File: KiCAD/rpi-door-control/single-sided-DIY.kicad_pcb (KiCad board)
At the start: 2 copper layers, 123 x 50 mm, 26 parts, among them IC1 4N35, J1 RJ45, P1 CONN_13X2, P2 CONN_2, P3 CONN_2, P4 CONN_2, Q1 2N3904, Q2 2N3904, SW1 SW_PUSH, U1 RELAY

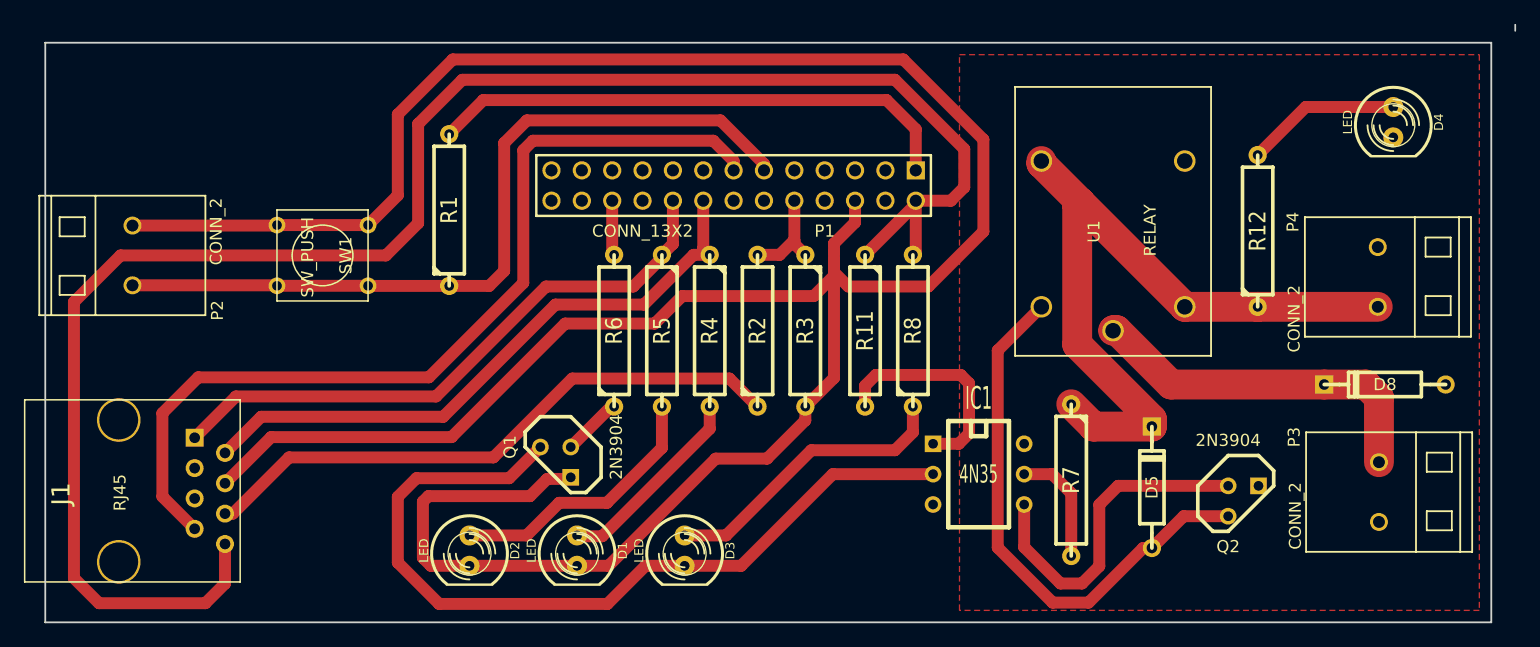
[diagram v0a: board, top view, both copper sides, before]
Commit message: Added silk screen text, drill holes, general polishing
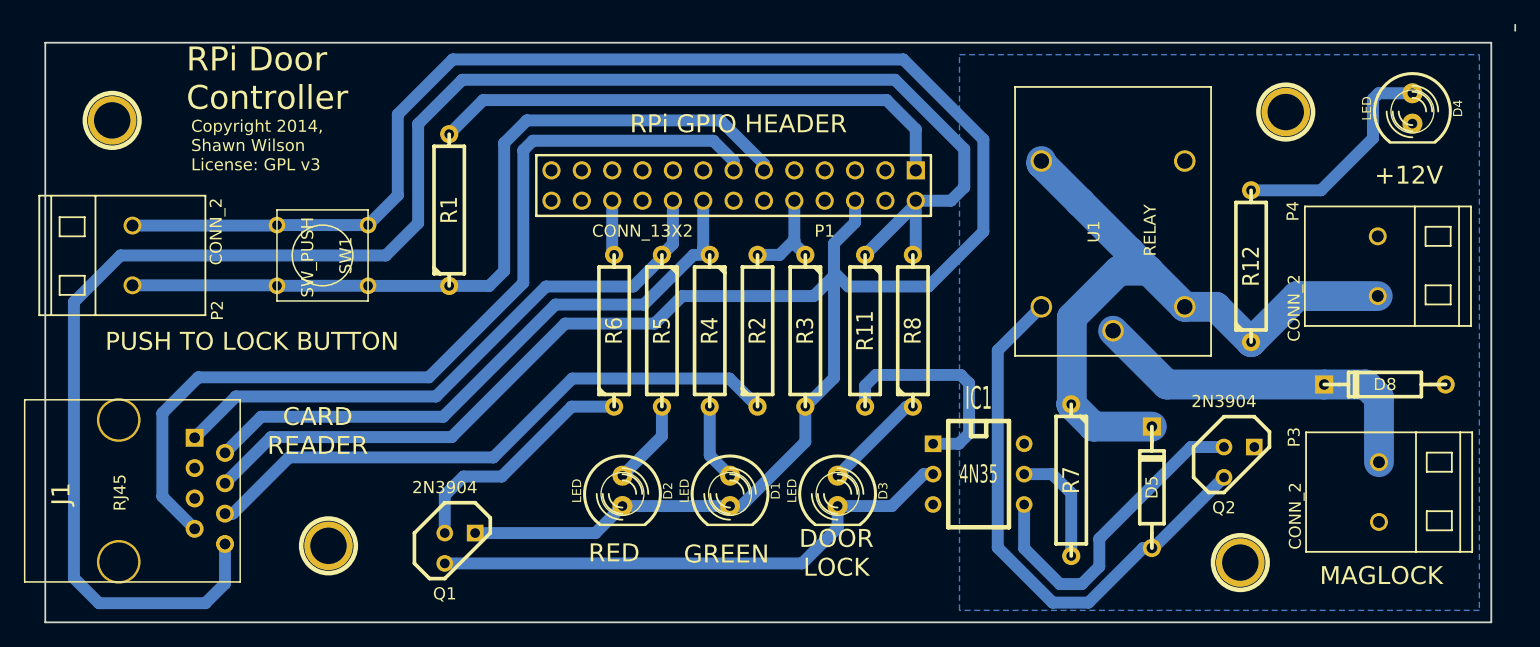
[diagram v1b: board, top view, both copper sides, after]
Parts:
- added ?: , 1pin, F.Cu at (180.0, 121.0)
- added ?: , 1pin, F.Cu at (103.7, 119.6)
- added ?: , 1pin, F.Cu at (183.8, 83.3)
- added ?: , 1pin, F.Cu at (85.6, 84.0)
- moved D1 13.7 mm to (137.3, 115.0)
- moved D2 13.7 mm to (128.3, 115.0)
- moved D3 13.7 mm to (146.3, 115.0)
- moved Q1 10.8 mm to (114.7, 119.8), turned to 0 degrees
- moved Q2 3.27 mm to (179.9, 112.6)
- moved R12 3.00 mm to (180.9, 96.2)
- moved D4 1.97 mm to (194.4, 83.0)
- moved P4 0.90 mm to (191.5, 96.2)
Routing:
- net N-0000025: track 69.9 -> 45.0 mm
- net GND: track 241.9 -> 219.2 mm
- net N-0000026: track 24.8 -> 8.69 mm
- net N-000001: track 22.6 -> 7.15 mm
- net N-000003: track 5.03 -> 20.4 mm
- net N-000002: track 16.7 -> 6.48 mm
- net N-0000021: track 13.0 -> 18.8 mm
- net +12V: track 62.3 -> 59.1 mm
- net N-0000038: track 45.8 -> 46.8 mm
- net N-0000020: track 28.3 -> 27.7 mm
- added copper zone on B.Cu, net GNDPWR
- removed copper zone on F.Cu, net GNDPWR
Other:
- board text added: "+12V"
- board text added: "CARD READER"
- board text added: "Copyright 2014, Shawn Wilson License: GPL v3"
- board text added: "DOOR LOCK"
- board text added: "GREEN"
- board text added: "MAGLOCK"
- board text added: "PUSH TO LOCK BUTTON"
- board text added: "RED"
- board text added: "RPi Door Controller"
- board text added: "RPi GPIO HEADER"

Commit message: Got 3D model for terminal blocks working.  Still need to change the colour of the skin but they do show up in the KiCAD 3D view.
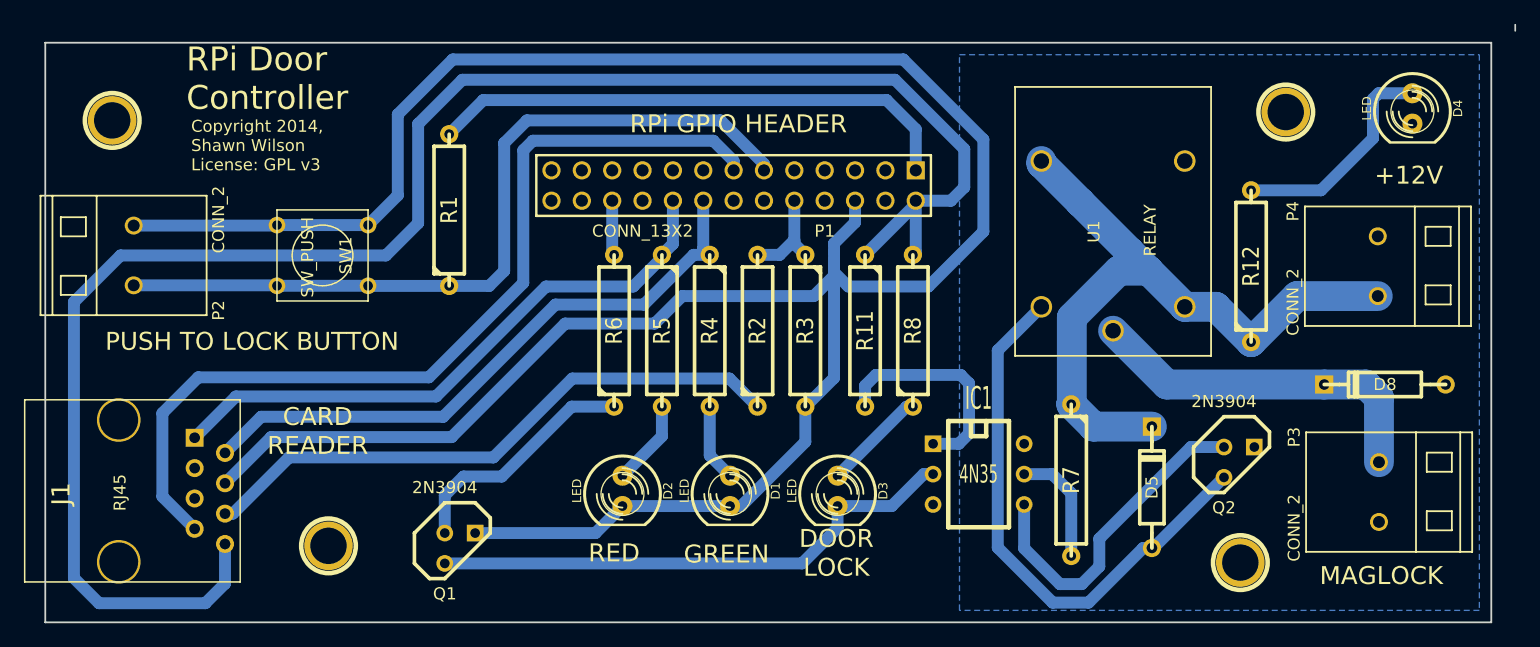
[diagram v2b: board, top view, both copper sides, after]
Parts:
- moved P2 0.10 mm to (87.4, 95.3)
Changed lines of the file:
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@@
     (links 48)
     (no_connects 0)
-    (area 77.712499 75.924999 203.075001 126.075001)
+    (area 79.924999 75.924999 203.075001 126.075001)
     (thickness 1.6)
     (drawings 15)
@@
     )
   )
+  (module DIP-6__300 (layer F.Cu)
+    (at 158.1 113.6 270)
+    (descr "6 pins DIL package, round pads")
+    (tags DIL)
+    (fp_text reference IC1 (at -6.35 0 360) (layer F.SilkS)
+      (effects (font (size 1.905 1.016) (thickness 0.2032)))
+    )
+    (fp_text value 4N35 (at 0 0 360) (layer F.SilkS)
+      (effects (font (size 1.524 0.889) (thickness 0.2032)))
+    )
+    (fp_line (start -4.445 -2.54) (end 4.445 -2.54) (layer F.SilkS) (width 0.381))
+    (fp_line (start 4.445 -2.54) (end 4.445 2.54) (layer F.SilkS) (width 0.381))
+    (fp_line (start 4.445 2.54) (end -4.445 2.54) (layer F.SilkS) (width 0.381))
+    (fp_line (start -4.445 2.54) (end -4.445 -2.54) (layer F.SilkS) (width 0.381))
+    (fp_line (start -4.445 -0.635) (end -3.175 -0.635) (layer F.SilkS) (width 0.381))
+    (fp_line (start -3.175 -0.635) (end -3.175 0.635) (layer F.SilkS) (width 0.381))
+    (fp_line (start -3.175 0.635) (end -4.445 0.635) (layer F.SilkS) (width 0.381))
+    (pad 1 thru_hole rect (at -2.54 3.81 270) (size 1.397 1.397) (drill 0.8128)
+      (layers *.Cu *.Mask F.SilkS)
+      (net 15 N-0000019)
+    )
+    (pad 2 thru_hole circle (at 0 3.81 270) (size 1.397 1.397) (drill 0.8128)
+      (layers *.Cu *.Mask F.SilkS)
+      (net 19 N-0000025)
+    )
+    (pad 3 thru_hole circle (at 2.54 3.81 270) (size 1.397 1.397) (drill 0.8128)
+      (layers *.Cu *.Mask F.SilkS)
+    )
+    (pad 4 thru_hole circle (at 2.54 -3.81 270) (size 1.397 1.397) (drill 0.8128)
+      (layers *.Cu *.Mask F.SilkS)
+      (net 17 N-0000020)
+    )
+    (pad 5 thru_hole circle (at 0 -3.81 270) (size 1.397 1.397) (drill 0.8128)
+      (layers *.Cu *.Mask F.SilkS)
+      (net 14 N-0000018)
+    )
+    (pad 6 thru_hole circle (at -2.54 -3.81 270) (size 1.397 1.397) (drill 0.8128)
+      (layers *.Cu *.Mask F.SilkS)
+    )
+    (model dil/dil_6.wrl
+      (at (xyz 0 0 0))
+      (scale (xyz 1 1 1))
+      (rotate (xyz 0 0 0))
+    )
+  )
+  (module 1pin (layer F.Cu)
+    (at 85.6 84)
+    (descr "module 1 pin (ou trou mecanique de percage)")
+    (tags DEV)
+    (path 1pin)
+    (clearance 2)
+    (fp_text reference "" (at 0 -3.048) (layer F.SilkS)
+      (effects (font (size 1.016 1.016) (thickness 0.254)))
+    )
+    (fp_text value "" (at 0 2.794) (layer F.SilkS) hide
+      (effects (font (size 1.016 1.016) (thickness 0.254)))
+    )
+    (fp_circle (center 0 0) (end 0 -2.286) (layer F.SilkS) (width 0.381))
+    (pad 1 thru_hole circle (at 0 0) (size 4.064 4.064) (drill 3.048)
+      (layers *.Cu *.Mask F.SilkS)
+    )
+  )
+  (module C2_KF103 (layer F.Cu)
+    (at 87.4 95.3 90)
+    (fp_text reference P2 (at -4.6 7.1 90) (layer F.SilkS)
+      (effects (font (size 1 1) (thickness 0.15)))
+    )
+    (fp_text value CONN_2 (at 3 7.1 90) (layer F.SilkS)
+      (effects (font (size 1 1) (thickness 0.15)))
+    )
+    (fp_line (start 3.2 -4) (end 1.6 -4) (layer F.SilkS) (width 0.15))
+    (fp_line (start 3.2 -6.1) (end 3.2 -4) (layer F.SilkS) (width 0.15))
+    (fp_line (start 1.6 -6.1) (end 3.2 -6.1) (layer F.SilkS) (width 0.15))
+    (fp_line (start 1.6 -4) (end 1.6 -6.1) (layer F.SilkS) (width 0.15))
+    (fp_line (start -3.3 -4) (end -3.3 -6.1) (layer F.SilkS) (width 0.15))
+    (fp_line (start -3.3 -6.1) (end -1.7 -6.1) (layer F.SilkS) (width 0.15))
+    (fp_line (start -1.7 -6.1) (end -1.7 -4) (layer F.SilkS) (width 0.15))
+    (fp_line (start -1.7 -4) (end -3.3 -4) (layer F.SilkS) (width 0.15))
+    (fp_line (start 5 -3.1) (end -5 -3.1) (layer F.SilkS) (width 0.15))
+    (fp_line (start 5 -6.8) (end -5 -6.8) (layer F.SilkS) (width 0.15))
+    (fp_line (start -5 -7.8) (end 5 -7.8) (layer F.SilkS) (width 0.15))
+    (fp_line (start 5 -7.8) (end 5 6.1) (layer F.SilkS) (width 0.15))
+    (fp_line (start 5 6.1) (end -5 6.1) (layer F.SilkS) (width 0.15))
+    (fp_line (start -5 6.1) (end -5 -7.8) (layer F.SilkS) (width 0.15))
+    (pad 1 thru_hole circle (at -2.5 0 90) (size 1.5 1.5) (drill 1)
+      (layers *.Cu *.Mask F.SilkS)
+      (net 5 /GPIO17)
+    )
+    (pad 2 thru_hole circle (at 2.5 0 90) (size 1.5 1.5) (drill 1)
+      (layers *.Cu *.Mask F.SilkS)
+      (net 11 GND)
+    )
+    (model 3D_models/KF103.wrl
+      (at (xyz 0.2 0.275 0))
+      (scale (xyz 0.393 0.393 0.393))
+      (rotate (xyz 90 0 90))
+    )
+  )
   (module C2_KF103 (layer F.Cu)
     (at 191.5 96.2 270)
@@
       (effects (font (size 1 1) (thickness 0.15)))
     )
-    (fp_text value CONN_2 (at 3.5 7 270) (layer F.SilkS)
+    (fp_text value CONN_2 (at 3 7.1 270) (layer F.SilkS)
       (effects (font (size 1 1) (thickness 0.15)))
     )
@@
       (net 1 +12V)
     )
+    (model 3D_models/KF103.wrl
+      (at (xyz 0.2 0.275 0))
+      (scale (xyz 0.393 0.393 0.393))
+      (rotate (xyz 90 0 90))
+    )
   )
   (module C2_KF103 (layer F.Cu)
@@
       (effects (font (size 1 1) (thickness 0.15)))
     )
-    (fp_text value CONN_2 (at 2 7 270) (layer F.SilkS)
+    (fp_text value CONN_2 (at 3 7.1 270) (layer F.SilkS)
       (effects (font (size 1 1) (thickness 0.15)))
     )
@@
       (net 12 GNDPWR)
     )
-  )
-  (module C2_KF103 (layer F.Cu)
-    (at 87.3 95.3 90)
-    (fp_text reference P2 (at -4.6 7.1 90) (layer F.SilkS)
-      (effects (font (size 1 1) (thickness 0.15)))
-    )
-    (fp_text value CONN_2 (at 2 7 90) (layer F.SilkS)
-      (effects (font (size 1 1) (thickness 0.15)))
-    )
-    (fp_line (start 3.2 -4) (end 1.6 -4) (layer F.SilkS) (width 0.15))
-    (fp_line (start 3.2 -6.1) (end 3.2 -4) (layer F.SilkS) (width 0.15))
-    (fp_line (start 1.6 -6.1) (end 3.2 -6.1) (layer F.SilkS) (width 0.15))
-    (fp_line (start 1.6 -4) (end 1.6 -6.1) (layer F.SilkS) (width 0.15))
-    (fp_line (start -3.3 -4) (end -3.3 -6.1) (layer F.SilkS) (width 0.15))
-    (fp_line (start -3.3 -6.1) (end -1.7 -6.1) (layer F.SilkS) (width 0.15))
-    (fp_line (start -1.7 -6.1) (end -1.7 -4) (layer F.SilkS) (width 0.15))
-    (fp_line (start -1.7 -4) (end -3.3 -4) (layer F.SilkS) (width 0.15))
-    (fp_line (start 5 -3.1) (end -5 -3.1) (layer F.SilkS) (width 0.15))
-    (fp_line (start 5 -6.8) (end -5 -6.8) (layer F.SilkS) (width 0.15))
-    (fp_line (start -5 -7.8) (end 5 -7.8) (layer F.SilkS) (width 0.15))
-    (fp_line (start 5 -7.8) (end 5 6.1) (layer F.SilkS) (width 0.15))
-    (fp_line (start 5 6.1) (end -5 6.1) (layer F.SilkS) (width 0.15))
-    (fp_line (start -5 6.1) (end -5 -7.8) (layer F.SilkS) (width 0.15))
-    (pad 1 thru_hole circle (at -2.5 0 90) (size 1.5 1.5) (drill 1)
-      (layers *.Cu *.Mask F.SilkS)
-      (net 5 /GPIO17)
-    )
-    (pad 2 thru_hole circle (at 2.5 0 90) (size 1.5 1.5) (drill 1)
-      (layers *.Cu *.Mask F.SilkS)
-      (net 11 GND)
-    )
-  )
-  (module DIP-6__300 (layer F.Cu)
-    (at 158.1 113.6 270)
-    (descr "6 pins DIL package, round pads")
-    (tags DIL)
-    (fp_text reference IC1 (at -6.35 0 360) (layer F.SilkS)
-      (effects (font (size 1.905 1.016) (thickness 0.2032)))
-    )
-    (fp_text value 4N35 (at 0 0 360) (layer F.SilkS)
-      (effects (font (size 1.524 0.889) (thickness 0.2032)))
-    )
-    (fp_line (start -4.445 -2.54) (end 4.445 -2.54) (layer F.SilkS) (width 0.381))
-    (fp_line (start 4.445 -2.54) (end 4.445 2.54) (layer F.SilkS) (width 0.381))
-    (fp_line (start 4.445 2.54) (end -4.445 2.54) (layer F.SilkS) (width 0.381))
-    (fp_line (start -4.445 2.54) (end -4.445 -2.54) (layer F.SilkS) (width 0.381))
-    (fp_line (start -4.445 -0.635) (end -3.175 -0.635) (layer F.SilkS) (width 0.381))
-    (fp_line (start -3.175 -0.635) (end -3.175 0.635) (layer F.SilkS) (width 0.381))
-    (fp_line (start -3.175 0.635) (end -4.445 0.635) (layer F.SilkS) (width 0.381))
-    (pad 1 thru_hole rect (at -2.54 3.81 270) (size 1.397 1.397) (drill 0.8128)
-      (layers *.Cu *.Mask F.SilkS)
-      (net 15 N-0000019)
-    )
-    (pad 2 thru_hole circle (at 0 3.81 270) (size 1.397 1.397) (drill 0.8128)
-      (layers *.Cu *.Mask F.SilkS)
-      (net 19 N-0000025)
-    )
-    (pad 3 thru_hole circle (at 2.54 3.81 270) (size 1.397 1.397) (drill 0.8128)
-      (layers *.Cu *.Mask F.SilkS)
-    )
-    (pad 4 thru_hole circle (at 2.54 -3.81 270) (size 1.397 1.397) (drill 0.8128)
-      (layers *.Cu *.Mask F.SilkS)
-      (net 17 N-0000020)
-    )
-    (pad 5 thru_hole circle (at 0 -3.81 270) (size 1.397 1.397) (drill 0.8128)
-      (layers *.Cu *.Mask F.SilkS)
-      (net 14 N-0000018)
-    )
-    (pad 6 thru_hole circle (at -2.54 -3.81 270) (size 1.397 1.397) (drill 0.8128)
-      (layers *.Cu *.Mask F.SilkS)
-    )
-    (model dil/dil_6.wrl
-      (at (xyz 0 0 0))
-      (scale (xyz 1 1 1))
-      (rotate (xyz 0 0 0))
-    )
-  )
-  (module 1pin (layer F.Cu)
-    (at 85.6 84)
-    (descr "module 1 pin (ou trou mecanique de percage)")
-    (tags DEV)
-    (path 1pin)
-    (clearance 2)
-    (fp_text reference "" (at 0 -3.048) (layer F.SilkS)
-      (effects (font (size 1.016 1.016) (thickness 0.254)))
-    )
-    (fp_text value "" (at 0 2.794) (layer F.SilkS) hide
-      (effects (font (size 1.016 1.016) (thickness 0.254)))
-    )
-    (fp_circle (center 0 0) (end 0 -2.286) (layer F.SilkS) (width 0.381))
-    (pad 1 thru_hole circle (at 0 0) (size 4.064 4.064) (drill 3.048)
-      (layers *.Cu *.Mask F.SilkS)
-    )
-  )
+    (model 3D_models/KF103.wrl
+      (at (xyz 0.2 0.275 0))
+      (scale (xyz 0.393 0.393 0.393))
+      (rotate (xyz 90 0 90))
+    )
+  )

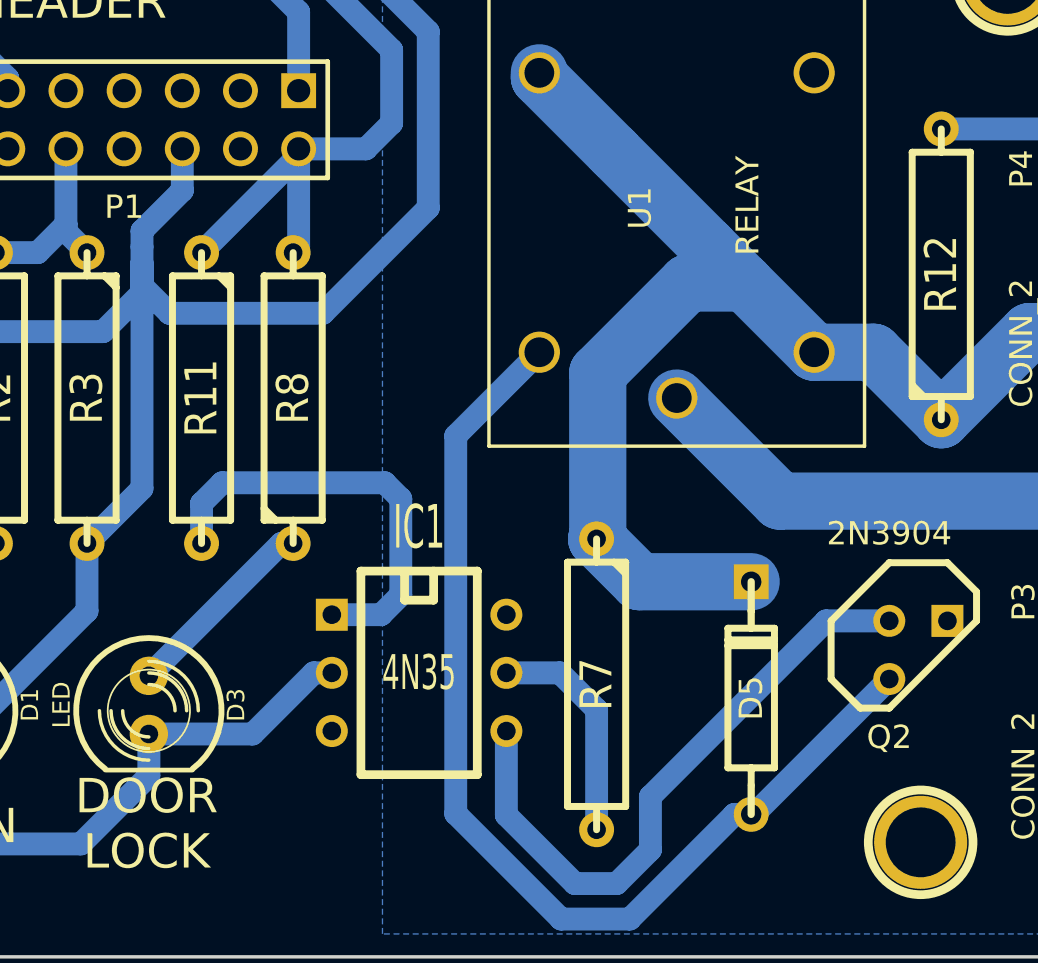
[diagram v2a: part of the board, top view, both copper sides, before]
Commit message: Swapped R8 and R11, maximized copper ground area for +12V and added a red LED to the custom footprints.
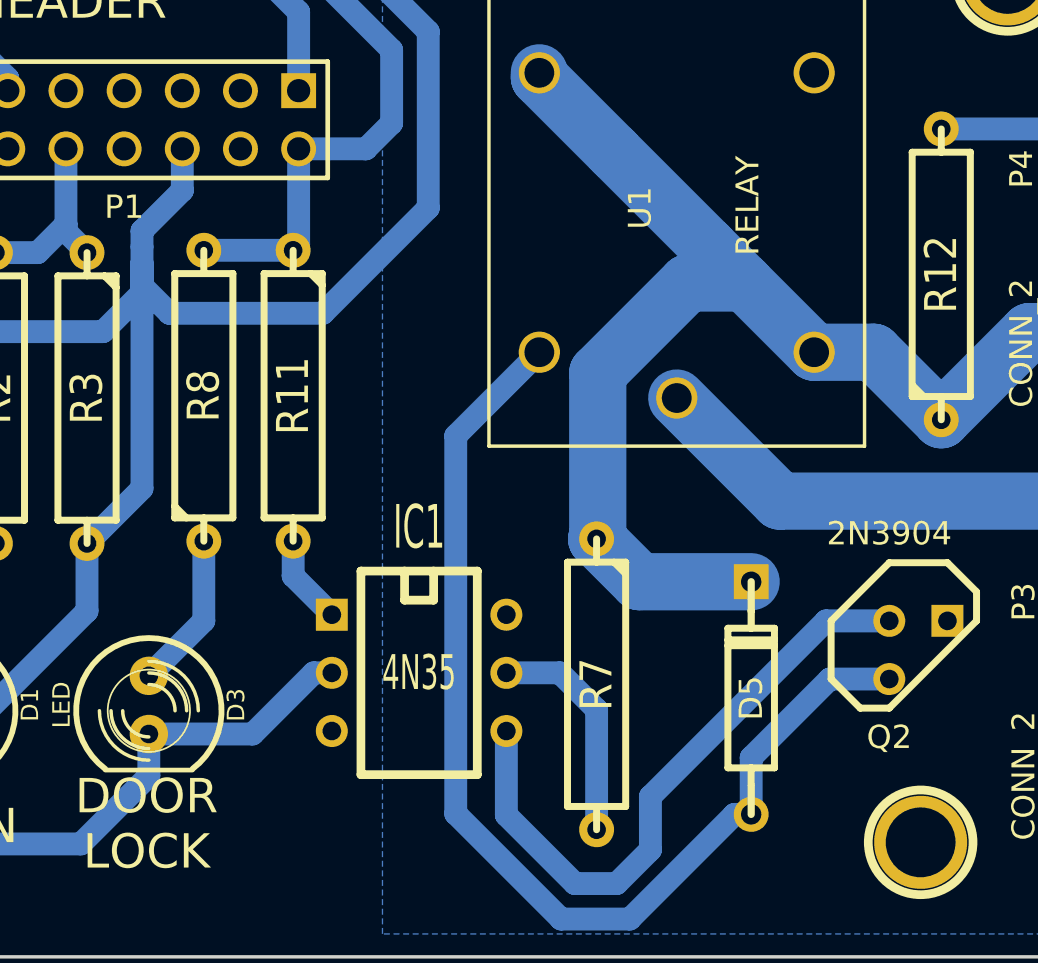
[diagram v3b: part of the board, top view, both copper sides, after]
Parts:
- moved R11 4.00 mm to (152.6, 101.5)
- moved R8 3.90 mm to (148.7, 101.5)
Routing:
- net N-0000019: track 18.7 -> 3.91 mm
- net +5V: track 148.7 -> 146.2 mm
- net N-0000026: track 8.69 -> 6.87 mm
- net N-0000038: track 46.8 -> 48.3 mm
